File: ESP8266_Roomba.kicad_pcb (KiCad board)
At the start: 2 copper layers, 3 parts, among them U1 TPS62177

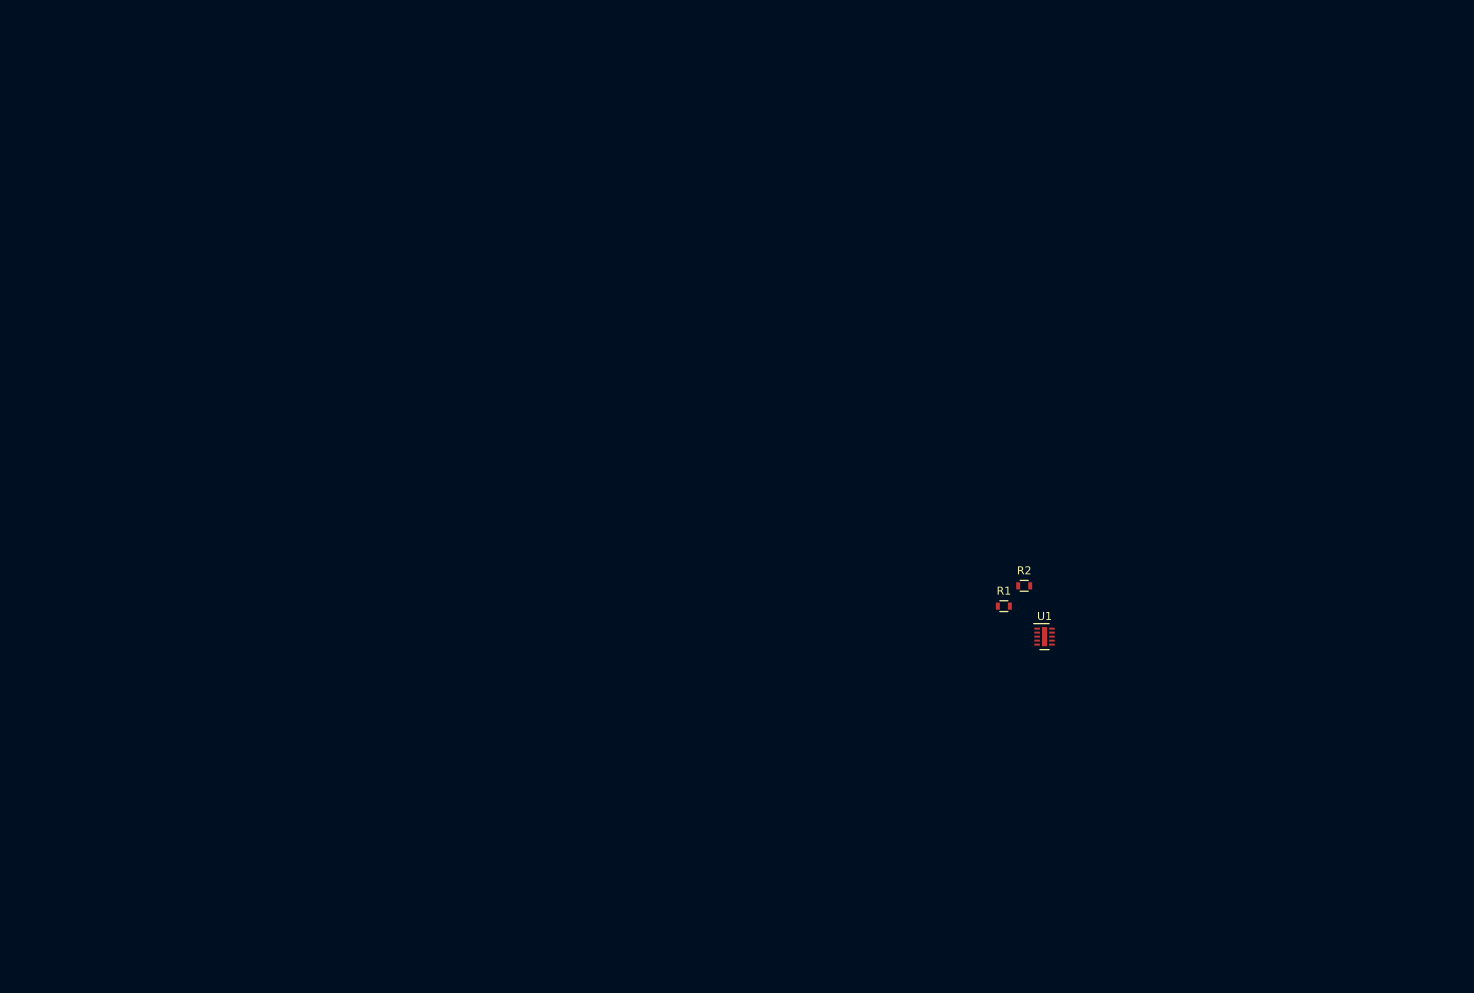
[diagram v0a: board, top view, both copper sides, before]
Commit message: Added alot of footprints
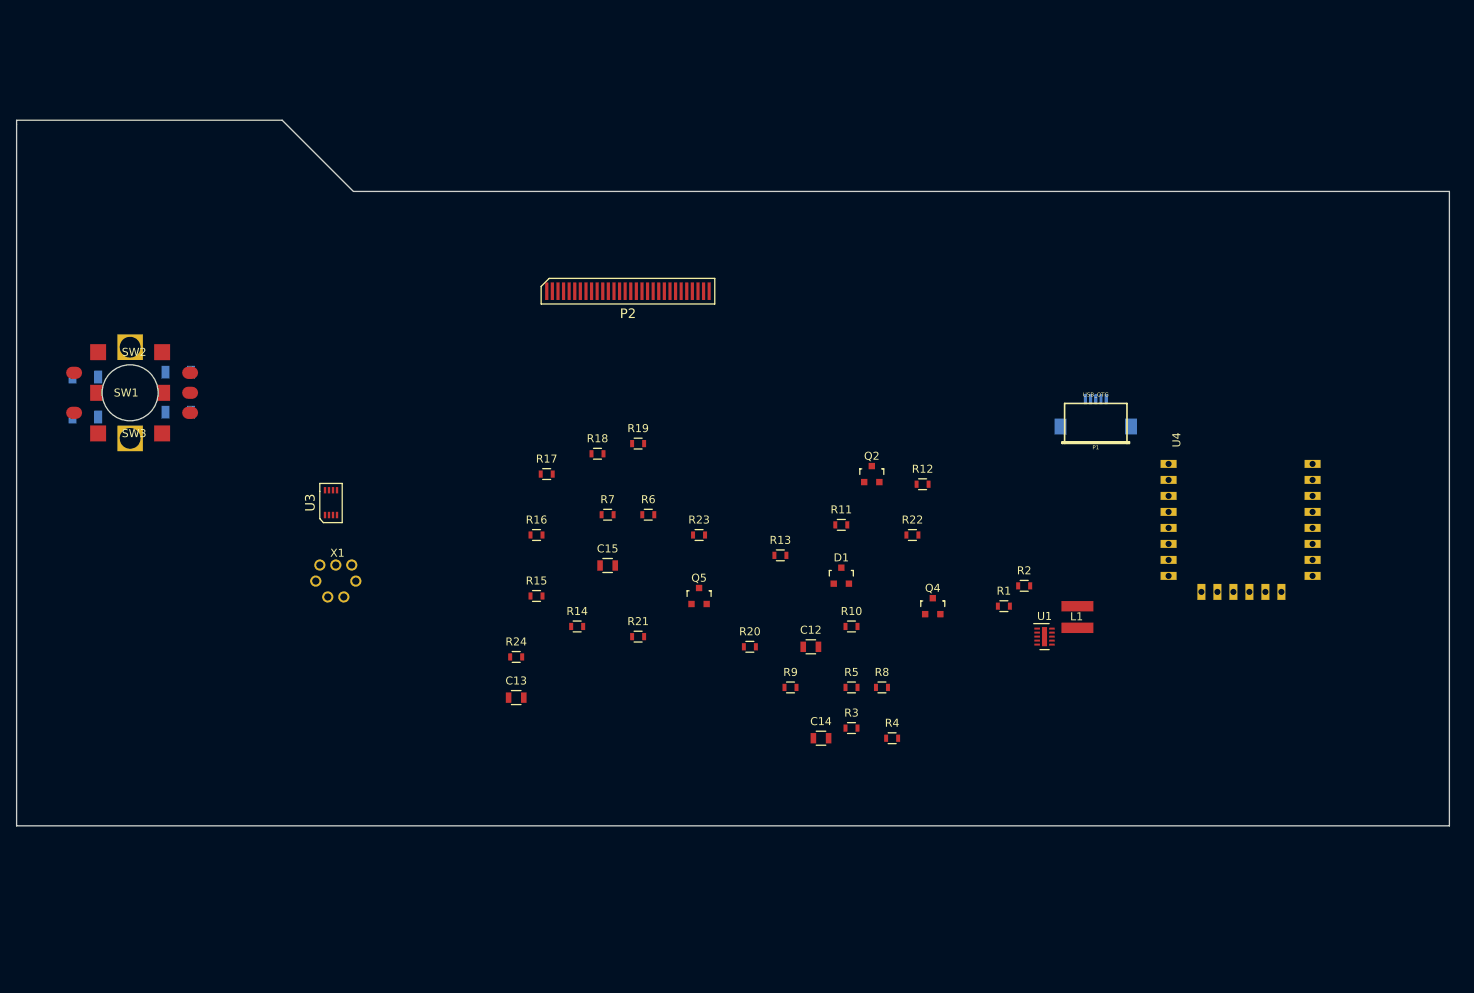
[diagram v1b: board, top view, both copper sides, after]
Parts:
- added C12: 1u, Resistors_SMD:R_0805, F.Cu at (119.4, 109.2)
- added C13: 1u, Resistors_SMD:R_0805, F.Cu at (82.5, 115.6)
- added C14: 2u2, Resistors_SMD:R_0805, F.Cu at (120.7, 120.7)
- added C15: 2u2, Resistors_SMD:R_0805, F.Cu at (94.0, 99.1)
- added D1: D_Schottky_x2_ACom_AKK, TO_SOT_Packages_SMD:SOT-23, F.Cu at (123.2, 100.3)
- added L1: VLS4012ET-100M, library:VLS4012ET-100M, F.Cu at (152.7, 105.5)
- added LED1: WS2812B, LEDs:LED_WS2812B-PLCC4, B.Cu at (28.7, 78.0)
- added LED2: WS2812B, LEDs:LED_WS2812B-PLCC4, B.Cu at (40.3, 77.4)
- added P1: USB_OTG, library:conn_usb_B_micro_smd-backside, F.Cu at (155.0, 81.7)
- added P2: UG_62864, library:UG_62864, F.Cu at (96.5, 64.8)
- added Q2: 2N7002, TO_SOT_Packages_SMD:SOT-23, F.Cu at (127.0, 87.6)
- added Q4: 2N7002, TO_SOT_Packages_SMD:SOT-23, F.Cu at (134.6, 104.1)
- added Q5: 2N7002, TO_SOT_Packages_SMD:SOT-23, F.Cu at (105.4, 102.9)
- added R10: 100k, Resistors_SMD:R_0603, F.Cu at (124.5, 106.7)
- added R11: 100k, Resistors_SMD:R_0603, F.Cu at (123.2, 94.0)
- added R12: 100k, Resistors_SMD:R_0603, F.Cu at (133.3, 88.9)
- added R13: 0R, Resistors_SMD:R_0603, F.Cu at (115.6, 97.8)
- added R14: 0R, Resistors_SMD:R_0603, F.Cu at (90.2, 106.7)
- added R15: 10k, Resistors_SMD:R_0603, F.Cu at (85.1, 102.9)
- added R16: 10k, Resistors_SMD:R_0603, F.Cu at (85.1, 95.2)
- added R17: 10k, Resistors_SMD:R_0603, F.Cu at (86.4, 87.6)
- added R18: 1k, Resistors_SMD:R_0603, F.Cu at (92.7, 85.1)
- added R19: 1k, Resistors_SMD:R_0603, F.Cu at (97.8, 83.8)
- added R20: 1k, Resistors_SMD:R_0603, F.Cu at (111.8, 109.2)
- added R21: 10k, Resistors_SMD:R_0603, F.Cu at (97.8, 108.0)
- added R22: 390k, Resistors_SMD:R_0603, F.Cu at (132.1, 95.2)
- added R23: 10k, Resistors_SMD:R_0603, F.Cu at (105.4, 95.2)
- added R24: 10k, Resistors_SMD:R_0603, F.Cu at (82.5, 110.5)
- added R3: 100k, Resistors_SMD:R_0603, F.Cu at (124.5, 119.4)
- added R4: 100k, Resistors_SMD:R_0603, F.Cu at (129.5, 120.7)
- added R5: 100k, Resistors_SMD:R_0603, F.Cu at (124.5, 114.3)
- added R6: 10k, Resistors_SMD:R_0603, F.Cu at (99.1, 92.7)
- added R7: 10k, Resistors_SMD:R_0603, F.Cu at (94.0, 92.7)
- added R8: 100k, Resistors_SMD:R_0603, F.Cu at (128.3, 114.3)
- added R9: 100k, Resistors_SMD:R_0603, F.Cu at (116.8, 114.3)
- added ROT_ENC1: AB2_ROTARY_ENCODER_W_SW, library:ROT_ENC_backside, B.Cu at (34.3, 77.5)
- added SW1: SW_PUSH, library:switch3x6_smd, F.Cu at (34.3, 77.5)
- added SW2: SW_PUSH, library:switch3x6_smd, F.Cu at (34.3, 72.4)
- added SW3: SW_PUSH, library:switch3x6_smd, F.Cu at (34.3, 82.5)
- added U3: 74LVC3G14, library:VSSOP-8, F.Cu at (59.4, 91.2)
- added U4: ESP-12E, library:ESP-12E_SideMounted, F.Cu at (165.1, 86.4)
- added X1: MINI_DIN_7, library:MiniDin-7, F.Cu at (60.0, 100.6)
- R1: value 100k -> 1M
- R2: value 100k -> 10k
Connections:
- R1 pad 1: +3V3 -> Net-(R1-Pad1)
- R1 pad 2: Net-(R1-Pad2) -> +3V3
- R2 pad 1: +3V3 -> /RTS
- R2 pad 2: Net-(R2-Pad2) -> Net-(Q1-Pad1)
- U1 pad 7: Net-(R1-Pad2) -> Net-(R3-Pad2)
- U1 pad 8: Net-(R2-Pad2) -> Net-(R4-Pad2)
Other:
- board outline added: 179.1 x 88.2 mm

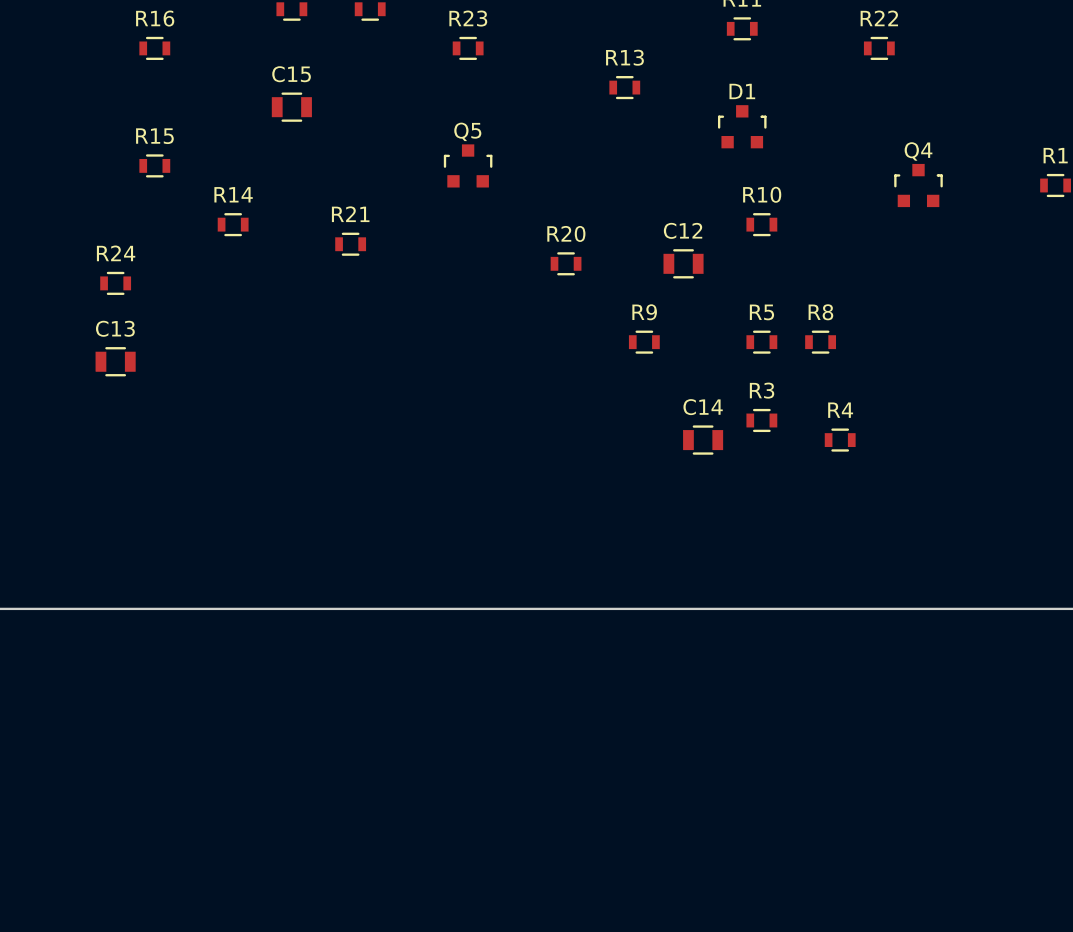
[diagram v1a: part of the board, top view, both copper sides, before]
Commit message: all footprints added
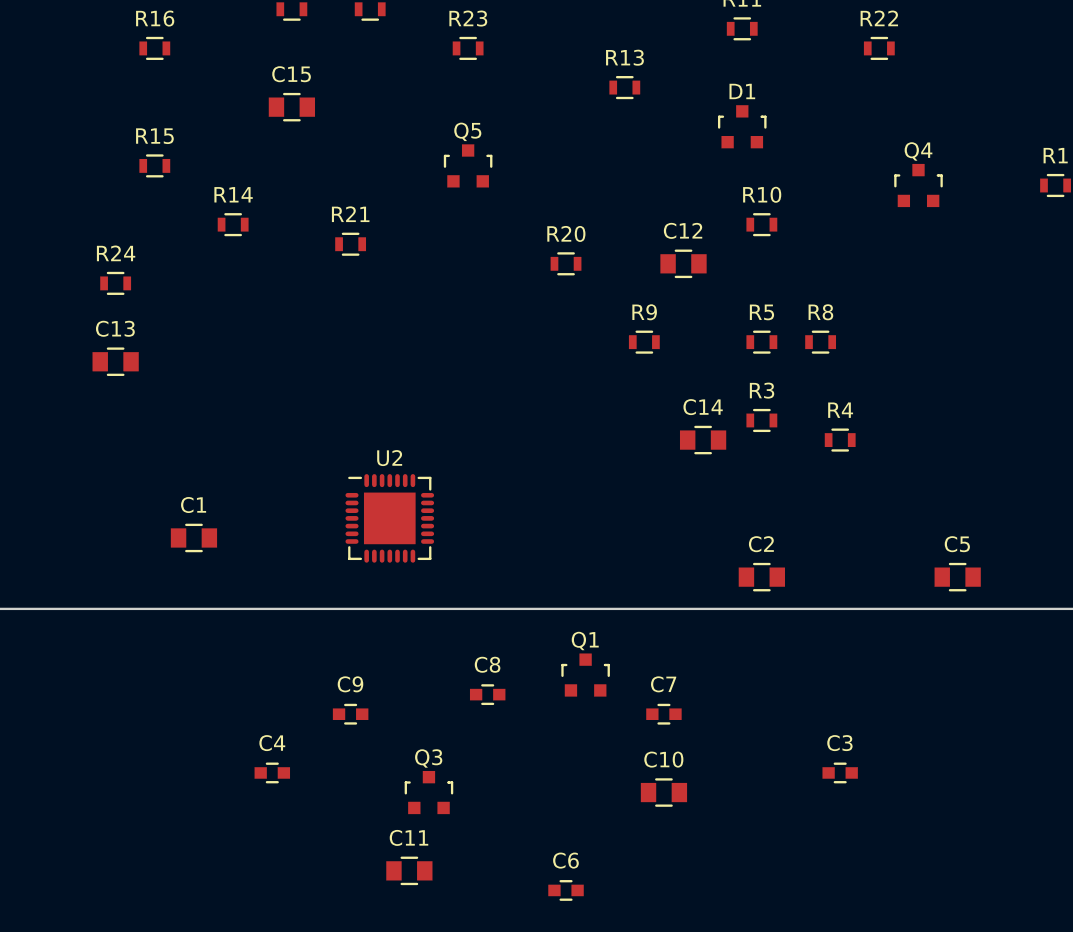
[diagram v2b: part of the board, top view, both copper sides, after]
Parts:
- added C1: 2u2, Capacitors_SMD:C_0805, F.Cu at (87.6, 127.0)
- added C10: 1u, Capacitors_SMD:C_0805, F.Cu at (118.1, 143.5)
- added C11: 2u2, Capacitors_SMD:C_0805, F.Cu at (101.6, 148.6)
- added C2: 1u, Capacitors_SMD:C_0805, F.Cu at (124.5, 129.5)
- added C3: 100n, Capacitors_SMD:C_0603, F.Cu at (129.5, 142.2)
- added C4: 100n, Capacitors_SMD:C_0603, F.Cu at (92.7, 142.2)
- added C5: 22u, Capacitors_SMD:C_0805, F.Cu at (137.2, 129.5)
- added C6: 100n, Capacitors_SMD:C_0603, F.Cu at (111.8, 149.9)
- added C7: 100n, Capacitors_SMD:C_0603, F.Cu at (118.1, 138.4)
- added C8: 100n, Capacitors_SMD:C_0603, F.Cu at (106.7, 137.2)
- added C9: 100n, Capacitors_SMD:C_0603, F.Cu at (97.8, 138.4)
- added Q1: BC849, TO_SOT_Packages_SMD:SOT-23, F.Cu at (113.0, 135.9)
- added Q3: BC849, TO_SOT_Packages_SMD:SOT-23, F.Cu at (102.9, 143.5)
- added U2: CP2102, library:QFN-28-1EP_5x5mm_Pitch0.5mm, F.Cu at (100.3, 125.7)
- C12, C13, C14, C15: footprint Resistors_SMD:R_0805 -> Capacitors_SMD:C_0805
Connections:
- D1 pad 3: Net-(D1-Pad3) -> (no net)
- LED2 pad 2: Net-(LED2-Pad2) -> (no net)
- P1 pad 4: Net-(P1-Pad4) -> (no net)
- P2 pad 21: Net-(P2-Pad21) -> (no net)
- P2 pad 22: Net-(P2-Pad22) -> (no net)
- P2 pad 23: Net-(P2-Pad23) -> (no net)
- P2 pad 24: Net-(P2-Pad24) -> (no net)
- P2 pad 25: Net-(P2-Pad25) -> (no net)
- P2 pad 7: Net-(P2-Pad7) -> (no net)
- R16 pad 2: Net-(R16-Pad2) -> (no net)
- R17 pad 2: Net-(R17-Pad2) -> (no net)
- R9 pad 2: Net-(R9-Pad2) -> (no net)
- U4 pad 10: Net-(U4-Pad10) -> (no net)
- U4 pad 11: Net-(U4-Pad11) -> (no net)
- U4 pad 12: Net-(U4-Pad12) -> (no net)
- U4 pad 13: Net-(U4-Pad13) -> (no net)
- U4 pad 14: Net-(U4-Pad14) -> (no net)
- U4 pad 9: Net-(U4-Pad9) -> (no net)

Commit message: some layout done
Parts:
- removed Q3: BC849, TO_SOT_Packages_SMD:SOT-23
- added C16: 100n, Capacitors_SMD:C_0603, F.Cu at (144.7, 55.4)
- added D2: D_Schottky_x2_ACom_AKK, TO_SOT_Packages_SMD:SOT-23, F.Cu at (133.7, 62.1)
- Q1: value BC849 -> DMC204010R; footprint TO_SOT_Packages_SMD:SOT-23 -> TO_SOT_Packages_SMD:SOT-23-6
- moved C4 98.4 mm to (132.5, 52.3), turned to 270 degrees
- moved X1 98.3 mm to (141.1, 45.0), turned to 90 degrees
- moved C3 93.2 mm to (134.2, 49.2)
- moved U3 90.6 mm to (142.6, 55.4), turned to 180 degrees
- moved C6 87.8 mm to (143.4, 68.0)
- moved C2 83.0 mm to (133.9, 47.1)
- moved U2 80.1 mm to (127.7, 50.5), turned to 180 degrees
- moved Q1 78.5 mm to (126.0, 58.4), turned to 90 degrees
- moved C1 75.9 mm to (134.3, 67.1), turned to 270 degrees
- moved U4 73.5 mm to (102.2, 48.3)
- moved C10 67.1 mm to (181.6, 121.9)
- moved C11 67.1 mm to (165.1, 127.0)
- moved C7 67.1 mm to (181.6, 116.8)
- moved C8 67.1 mm to (170.2, 115.6)
- moved C9 67.1 mm to (161.3, 116.8)
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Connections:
- Q1 pad 1: Net-(Q1-Pad1) -> /DTR
- Q1 pad 2: /DTR -> Net-(Q1-Pad2)
- Q1 pad 3: /Switch -> /RST
- R2 pad 2: Net-(Q1-Pad1) -> Net-(Q1-Pad2)
- R6 pad 2: Net-(Q3-Pad1) -> Net-(Q1-Pad5)
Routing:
- net +3V3: track 0.00 -> 81.5 mm, vias 0 -> 2
- net GND: track 0.00 -> 62.5 mm, vias 0 -> 9
- net /ADC: track 0.00 -> 54.1 mm, vias 0 -> 1
- net +12V: track 0.00 -> 48.9 mm, vias 0 -> 1
- net /TXD: track 0.00 -> 39.1 mm, vias 0 -> 4
- net /RXD: track 0.00 -> 38.7 mm, vias 0 -> 1
- net /Roomba_Wake: track 0.00 -> 27.6 mm, vias 0 -> 2
- net /DTR: track 0.00 -> 16.4 mm, vias 0 -> 2
- net Net-(R1-Pad1): track 0.00 -> 13.3 mm, vias 0 -> 2
- net +5V: track 0.00 -> 10.7 mm, vias 0 -> 1
- net Net-(D1-Pad2): track 0.00 -> 9.57 mm, vias 0 -> 2
- net Net-(Q2-Pad3): track 0.00 -> 7.68 mm
- net Net-(P1-Pad3): track 0.00 -> 7.34 mm, vias 0 -> 1
- net Net-(Q4-Pad3): track 0.00 -> 7.32 mm
- net Net-(Q4-Pad1): track 0.00 -> 7.00 mm
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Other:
- board size 179.1 x 88.2 mm -> 100 x 30 mm
- net class high current added: clearance 0.2, trace_width 0.8, via_dia 0.6, via_drill 0.4
- net class small added: clearance 0.2, trace_width 0.15, via_dia 0.6, via_drill 0.4
- rule trace_min: 0.2 -> 0.15

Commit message: more layout done
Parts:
- added C17: 100n, Capacitors_SMD:C_0603, F.Cu at (65.7, 33.3)
- added R25: 0R, Resistors_SMD:R_0603, F.Cu at (69.5, 33.3)
- added R26: 0R, Resistors_SMD:R_0603, F.Cu at (73.0, 33.3)
- moved C8 138.5 mm to (50.6, 45.8), turned to 270 degrees
- moved C7 132.3 mm to (66.9, 51.0), turned to 180 degrees
- moved C9 122.5 mm to (50.4, 64.8), turned to 90 degrees
- moved C10 118.1 mm to (84.0, 55.5), turned to 270 degrees
- moved C11 115.3 mm to (74.7, 55.5), turned to 90 degrees
- moved R20 74.3 mm to (52.3, 64.7), turned to 270 degrees
- moved C14 73.8 mm to (86.1, 55.5), turned to 90 degrees
- moved R9 72.4 mm to (67.3, 61.5), turned to 270 degrees
- moved R22 68.2 mm to (76.7, 55.5), turned to 90 degrees
- moved R13 63.0 mm to (60.4, 67.3)
- moved C13 59.7 mm to (89.0, 56.2), turned to 180 degrees
- moved C12 59.3 mm to (92.7, 56.2), turned to 180 degrees
- moved R19 59.2 mm to (52.5, 45.8), turned to 90 degrees
- moved R16 58.3 mm to (54.4, 45.8), turned to 270 degrees
- moved Q5 58.1 mm to (64.6, 61.5), turned to 90 degrees
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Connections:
- net +5V renamed /5V
- LED1 pad 4: /LED -> Net-(LED1-Pad4)
- R16 pad 2: (no net) -> +3V3
- R17 pad 2: (no net) -> +3V3
- R8 pad 1: +3V3 -> (no net)
- R9 pad 2: (no net) -> /PowerOn
- U4 pad 3: +3V3 -> (no net)
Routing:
- net /5V: track 10.7 -> 103.6 mm, vias 1 -> 4
- net GND: track 62.5 -> 144.9 mm, vias 9 -> 18
- net /Enc_A: track 0.00 -> 79.8 mm, vias 0 -> 1
- net /Switch: track 6.30 -> 69.9 mm, vias 1 -> 2
- net /PowerOn: track 0.00 -> 55.0 mm, vias 0 -> 2
- net /RST: track 0.00 -> 51.4 mm, vias 0 -> 2
- net +3V3: track 81.5 -> 124.6 mm, vias 2 -> 5
- net /LED: track 0.00 -> 39.7 mm, vias 0 -> 1
- net /Enc_B: track 0.00 -> 39.2 mm
- net /ADC: track 54.1 -> 66.3 mm, vias 1 -> 3
- net Net-(R7-Pad1): track 0.00 -> 11.7 mm, vias 0 -> 2
- net Net-(R19-Pad1): track 0.00 -> 9.70 mm
- net /SDA: track 0.00 -> 9.55 mm, vias 0 -> 1
- net Net-(R20-Pad1): track 0.00 -> 9.04 mm
- net Net-(C10-Pad2): track 0.00 -> 7.97 mm
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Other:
- outline, holes or cut-outs redrawn

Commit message: layout done
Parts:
- added P3: CONN_01X04, Pin_Headers:Pin_Header_Straight_1x04, F.Cu at (133.4, 74.0)
- added P4: CONN_01X02, Pin_Headers:Pin_Header_Straight_1x02, F.Cu at (177.1, 72.8)
- added P5: CONN_01X07, Pin_Headers:Pin_Header_Straight_1x07, F.Cu at (150.6, 77.8)
- added U5: 74LVC3G14, library:VSSOP-8, F.Cu at (125.3, 77.5)
- moved R25 76.6 mm to (130.6, 79.5), turned to 180 degrees
- moved C17 75.6 mm to (125.3, 79.8)
- moved R26 72.7 mm to (130.6, 77.8), turned to 180 degrees
- moved L1 61.7 mm to (180.9, 97.2)
- moved R15 61.7 mm to (176.8, 98.2)
- moved R23 61.7 mm to (134.3, 85.2)
- moved R3 61.7 mm to (181.0, 92.3)
- moved C9 61.7 mm to (104.4, 94.5)
- moved R13 61.7 mm to (114.4, 97.2)
- moved R14 61.7 mm to (111.4, 97.2)
- moved R16 61.7 mm to (108.4, 75.5)
- moved ROT_ENC1 61.7 mm to (110.3, 85.1)
- moved SW1 61.7 mm to (110.3, 85.1)
- moved C1 61.7 mm to (188.3, 96.9)
- moved C10 61.7 mm to (138.0, 85.2)
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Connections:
- R26 pad 2: (no net) -> Net-(R26-Pad2)
- ROT_ENC1 pad 7: Net-(ROT_ENC1-Pad7) -> GND
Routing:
- net +3V3: track 124.6 -> 234.7 mm, vias 5 -> 7
- net GND: track 144.9 -> 197.8 mm, vias 18 -> 28
- net GNDPWR: track 0.00 -> 48.1 mm, vias 0 -> 4
- net /SDA: track 9.55 -> 57.0 mm, vias 1 -> 3
- net Net-(LED1-Pad1): track 0.00 -> 44.8 mm, vias 0 -> 1
- net /SCL: track 6.59 -> 50.0 mm, vias 1 -> 3
- net /LED: track 39.7 -> 79.5 mm, vias 1 -> 4
- net Net-(LED1-Pad4): track 0.00 -> 25.7 mm, vias 0 -> 1
- net /Enc_B: track 39.2 -> 64.5 mm, vias 0 -> 3
- net /5V: track 103.6 -> 127.0 mm, vias 4 -> 7
- net /PowerOn: track 55.0 -> 77.9 mm, vias 2 -> 4
- net Net-(LED1-Pad2): track 0.00 -> 20.1 mm, vias 0 -> 2
- net /Switch: track 69.9 -> 88.9 mm, vias 2 -> 4
- net /TXD: track 37.7 -> 45.3 mm
- net /RXD: track 37.3 -> 44.3 mm
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- added copper zone on B.Cu, net GND
- added copper zone on F.Cu, net GND
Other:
- outline, holes or cut-outs redrawn
- board text added: "ESP8266"
- board text added: "LiLu 2016-05-09"
- board text added: "Roomba"

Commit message: Finished, commit before creating a panel
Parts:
- added P6: CONN_01X02, Pin_Headers:Pin_Header_Straight_1x02, F.Cu at (184.6, 89.8)
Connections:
- R8 pad 1: (no net) -> +3V3
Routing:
- net /Switch: track 88.9 -> 98.7 mm
- net GND: track 197.8 -> 206.4 mm, vias 28 -> 34
- net (no net): track 1.75 -> 0.00 mm
- net /Enc_A: track 86.6 -> 87.8 mm
- net /Roomba_Wake: track 27.8 -> 28.8 mm
- net /LED: track 79.5 -> 80.0 mm
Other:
- outline, holes or cut-outs redrawn
